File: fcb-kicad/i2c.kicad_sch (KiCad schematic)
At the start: 1 part

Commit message: hierarchic schemas, paljon muuta kivaa
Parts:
- added J3: Conn_01x04_Male, symbol Connector:Conn_01x04_Male
- added R10, R9: 10k, Resistor_SMD:R_0603_1608Metric, symbol Device:R_Small
- gave numbers to parts that had none: 1
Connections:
- new net +3V3: J3.1 (Pin_1), R10.1, R9.1
- new net GND: J3.4 (Pin_4)
- new net I2C1_SCL: J3.2 (Pin_2), J3.3 (Pin_3), R9.2
- new net I2C1_SDA: R10.2
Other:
- note added: "Connector for external I2C devices"
- note added: "Pullups for I2C lines"
- company: (none) -> University of Oulu
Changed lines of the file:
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@@
 (kicad_sch (version 20211123) (generator eeschema)
   (paper "A4")
+  (title_block
+    (company "University of Oulu")
+    (comment 1 "Antti Luukkonen, Jouni Saari, Visa Tuominen")
+  )
+  (wire (pts (xy 45.72 40.64) (xy 45.72 33.02))
+    (stroke (width 0) (type default) (color 0 0 0 0))
+  )
+  (wire (pts (xy 67.945 30.48) (xy 71.12 30.48))
+    (stroke (width 0) (type default) (color 0 0 0 0))
+  )
+  (wire (pts (xy 71.12 38.1) (xy 67.945 38.1))
+    (stroke (width 0) (type default) (color 0 0 0 0))
+  )
+  (wire (pts (xy 38.1 35.56) (xy 38.1 33.02))
+    (stroke (width 0) (type default) (color 0 0 0 0))
+  )
+  (wire (pts (xy 67.945 38.1) (xy 67.945 39.37))
+    (stroke (width 0) (type default) (color 0 0 0 0))
+  )
+  (wire (pts (xy 67.945 29.21) (xy 67.945 30.48))
+    (stroke (width 0) (type default) (color 0 0 0 0))
+  )
+  (wire (pts (xy 34.29 35.56) (xy 38.1 35.56))
+    (stroke (width 0) (type default) (color 0 0 0 0))
+  )
+  (wire (pts (xy 34.29 40.64) (xy 45.72 40.64))
+    (stroke (width 0) (type default) (color 0 0 0 0))
+  )
+  (text "Pullups for I2C lines\n" (at 22.86 21.59 0)
+    (effects (font (size 1.27 1.27)) (justify left bottom))
+  )
+  (text "Connector for external I2C devices" (at 58.42 21.59 0)
+    (effects (font (size 1.27 1.27)) (justify left bottom))
+  )
+  (global_label "I2C1_SCL" (shape input) (at 71.12 33.02 180) (fields_autoplaced)
+    (effects (font (size 1.27 1.27)) (justify right))
+    (property "Intersheet References" "${INTERSHEET_REFS}" (id 0) (at 59.9379 32.9406 0)
+      (effects (font (size 1.27 1.27)) (justify right) hide)
+    )
+  )
+  (global_label "I2C1_SCL" (shape input) (at 34.29 35.56 180) (fields_autoplaced)
+    (effects (font (size 1.27 1.27)) (justify right))
+    (property "Intersheet References" "${INTERSHEET_REFS}" (id 0) (at 23.1079 35.4806 0)
+      (effects (font (size 1.27 1.27)) (justify right) hide)
+    )
+  )
+  (global_label "I2C1_SCL" (shape input) (at 71.12 35.56 180) (fields_autoplaced)
+    (effects (font (size 1.27 1.27)) (justify right))
+    (property "Intersheet References" "${INTERSHEET_REFS}" (id 0) (at 59.9379 35.4806 0)
+      (effects (font (size 1.27 1.27)) (justify right) hide)
+    )
+  )
+  (global_label "I2C1_SDA" (shape input) (at 34.29 40.64 180) (fields_autoplaced)
+    (effects (font (size 1.27 1.27)) (justify right))
+    (property "Intersheet References" "${INTERSHEET_REFS}" (id 0) (at 23.0474 40.5606 0)
+      (effects (font (size 1.27 1.27)) (justify right) hide)
+    )
+  )
+  (symbol (lib_id "Device:R_Small") (at 38.1 30.48 0) (unit 1)
+    (in_bom yes) (on_board yes) (fields_autoplaced)
+    (property "Reference" "R9" (id 0) (at 39.5986 29.5715 0)
+      (effects (font (size 1.27 1.27)) (justify left))
+    )
+    (property "Value" "10k" (id 1) (at 39.5986 32.3466 0)
+      (effects (font (size 1.27 1.27)) (justify left))
+    )
+    (property "Footprint" "Resistor_SMD:R_0603_1608Metric" (id 2) (at 38.1 30.48 0)
+      (effects (font (size 1.27 1.27)) hide)
+    )
+    (property "Datasheet" "~" (id 3) (at 38.1 30.48 0)
+      (effects (font (size 1.27 1.27)) hide)
+    )
+    (property "LCSC" "C25804" (id 4) (at 38.1 30.48 0)
+      (effects (font (size 1.27 1.27)) hide)
+    )
+    (pin "1")
+    (pin "2")
+  )
+  (symbol (lib_id "power:+3.3V") (at 38.1 27.94 0) (unit 1)
+    (in_bom yes) (on_board yes) (fields_autoplaced)
+    (property "Reference" "#PWR021" (id 0) (at 38.1 31.75 0)
+      (effects (font (size 1.27 1.27)) hide)
+    )
+    (property "Value" "+3.3V" (id 1) (at 38.1 24.3355 0))
+    (property "Footprint" "" (id 2) (at 38.1 27.94 0)
+      (effects (font (size 1.27 1.27)) hide)
+    )
+    (property "Datasheet" "" (id 3) (at 38.1 27.94 0)
+      (effects (font (size 1.27 1.27)) hide)
+    )
+    (pin "1")
+  )
   (symbol (lib_id "000_sjt:BMP388") (at 80.01 74.93 0) (unit 1)
     (in_bom yes) (on_board yes) (fields_autoplaced)
-    (property "Reference" "U?" (id 0) (at 80.01 52.07 0))
+    (property "Reference" "U8" (id 0) (at 80.01 52.07 0))
     (property "Value" "BMP388" (id 1) (at 80.01 54.61 0))
     (property "Footprint" "000_sjt:PQFN50P200X200X80-10N" (id 2) (at 80.01 57.15 0))
@@
     (pin "9")
   )
+  (symbol (lib_id "power:GND") (at 67.945 39.37 0) (unit 1)
+    (in_bom yes) (on_board yes) (fields_autoplaced)
+    (property "Reference" "#PWR031" (id 0) (at 67.945 45.72 0)
+      (effects (font (size 1.27 1.27)) hide)
+    )
+    (property "Value" "GND" (id 1) (at 67.945 43.9325 0))
+    (property "Footprint" "" (id 2) (at 67.945 39.37 0)
+      (effects (font (size 1.27 1.27)) hide)
+    )
+    (property "Datasheet" "" (id 3) (at 67.945 39.37 0)
+      (effects (font (size 1.27 1.27)) hide)
+    )
+    (pin "1")
+  )
+  (symbol (lib_id "power:+3.3V") (at 45.72 27.94 0) (unit 1)
+    (in_bom yes) (on_board yes) (fields_autoplaced)
+    (property "Reference" "#PWR024" (id 0) (at 45.72 31.75 0)
+      (effects (font (size 1.27 1.27)) hide)
+    )
+    (property "Value" "+3.3V" (id 1) (at 45.72 24.3355 0))
+    (property "Footprint" "" (id 2) (at 45.72 27.94 0)
+      (effects (font (size 1.27 1.27)) hide)
+    )
+    (property "Datasheet" "" (id 3) (at 45.72 27.94 0)
+      (effects (font (size 1.27 1.27)) hide)
+    )
+    (pin "1")
+  )
+  (symbol (lib_id "Connector:Conn_01x04_Male") (at 76.2 33.02 0) (mirror y) (unit 1)
+    (in_bom yes) (on_board yes) (fields_autoplaced)
+    (property "Reference" "J3" (id 0) (at 76.9112 33.3815 0)
+      (effects (font (size 1.27 1.27)) (justify right))
+    )
+    (property "Value" "Conn_01x04_Male" (id 1) (at 76.9112 36.1566 0)
+      (effects (font (size 1.27 1.27)) (justify right))
+    )
+    (property "Footprint" "" (id 2) (at 76.2 33.02 0)
+      (effects (font (size 1.27 1.27)) hide)
+    )
+    (property "Datasheet" "~" (id 3) (at 76.2 33.02 0)
+      (effects (font (size 1.27 1.27)) hide)
+    )
+    (pin "1")
+    (pin "2")
+    (pin "3")
+    (pin "4")
+  )
+  (symbol (lib_id "Device:R_Small") (at 45.72 30.48 0) (unit 1)
+    (in_bom yes) (on_board yes) (fields_autoplaced)
+    (property "Reference" "R10" (id 0) (at 47.2186 29.5715 0)
+      (effects (font (size 1.27 1.27)) (justify left))
+    )
+    (property "Value" "10k" (id 1) (at 47.2186 32.3466 0)
+      (effects (font (size 1.27 1.27)) (justify left))
+    )
+    (property "Footprint" "Resistor_SMD:R_0603_1608Metric" (id 2) (at 45.72 30.48 0)
+      (effects (font (size 1.27 1.27)) hide)
+    )
+    (property "Datasheet" "~" (id 3) (at 45.72 30.48 0)
+      (effects (font (size 1.27 1.27)) hide)
+    )
+    (property "LCSC" "C25804" (id 4) (at 45.72 30.48 0)
+      (effects (font (size 1.27 1.27)) hide)
+    )
+    (pin "1")
+    (pin "2")
+  )
+  (symbol (lib_id "power:+3.3V") (at 67.945 29.21 0) (unit 1)
+    (in_bom yes) (on_board yes) (fields_autoplaced)
+    (property "Reference" "#PWR025" (id 0) (at 67.945 33.02 0)
+      (effects (font (size 1.27 1.27)) hide)
+    )
+    (property "Value" "+3.3V" (id 1) (at 67.945 25.6055 0))
+    (property "Footprint" "" (id 2) (at 67.945 29.21 0)
+      (effects (font (size 1.27 1.27)) hide)
+    )
+    (property "Datasheet" "" (id 3) (at 67.945 29.21 0)
+      (effects (font (size 1.27 1.27)) hide)
+    )
+    (pin "1")
+  )
 )

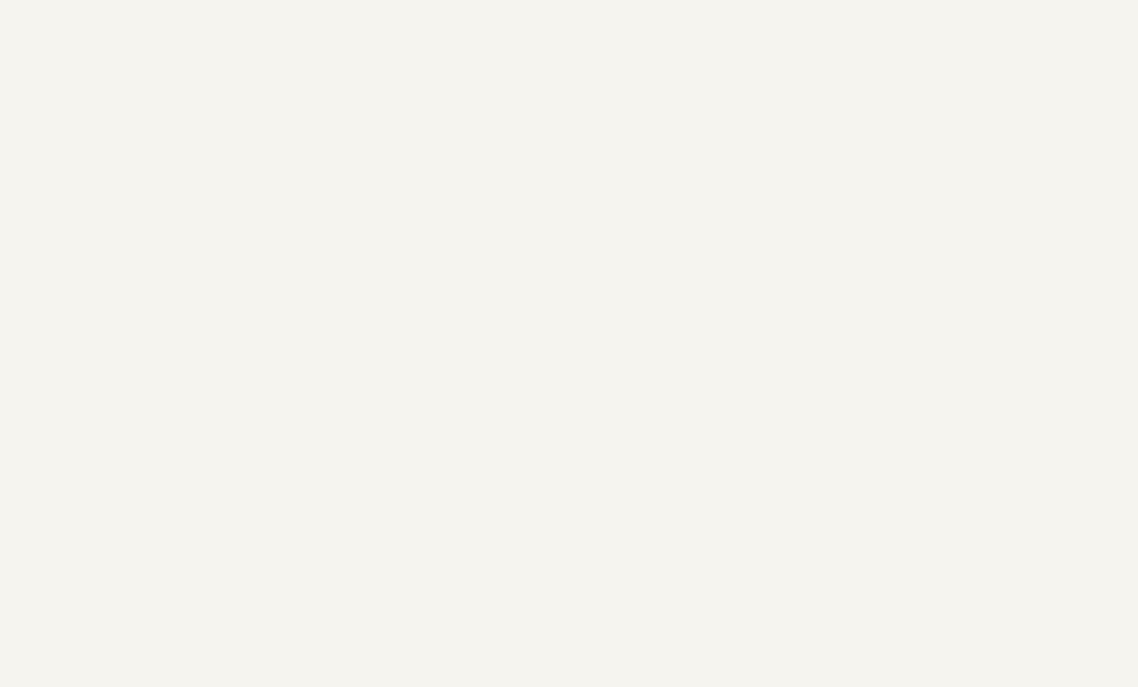
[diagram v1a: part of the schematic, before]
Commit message: 4in1 connector library part, SPI CS pullups, migrate magnetometer cirtuit
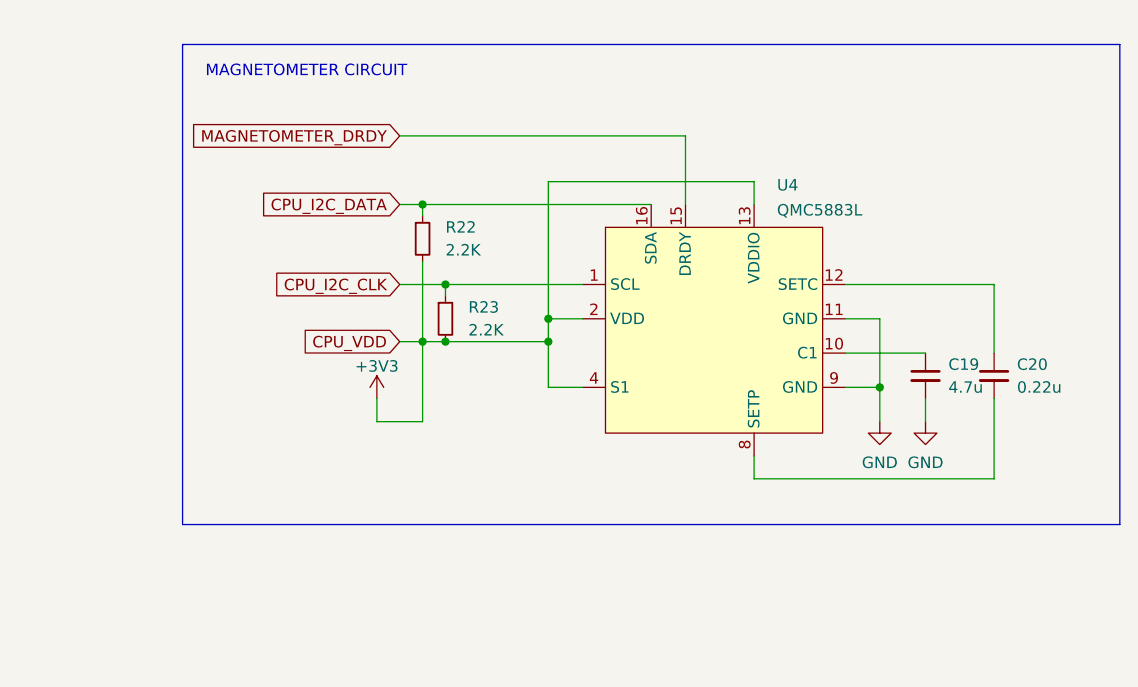
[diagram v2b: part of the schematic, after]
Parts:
- added C19: 4.7u, symbol Device:C_Small
- added C20: 0.22u, symbol Device:C_Small
- added R22, R23: 2.2K, symbol Device:R_Small
- added U4: QMC5883L, symbol 000_sjt:QMC5883L
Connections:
- net +3V3: now also R22.2, R23.2, U4.13 (VDDIO), U4.2 (VDD), U4.4 (S1)
- net GND: now also C19.2, U4.11 (GND), U4.9 (GND)
- new net: C19.1, U4.10 (C1)
- new net: C20.1, U4.12 (SETC)
- new net: C20.2, U4.8 (SETP)
- new net CPU_I2C_CLK: R23.1, U4.1 (SCL)
- new net CPU_I2C_DATA: R22.1, U4.16 (SDA)
- new net MAGNETOMETER_DRDY: U4.15 (DRDY)
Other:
- note added: "MAGNETOMETER CIRCUIT"

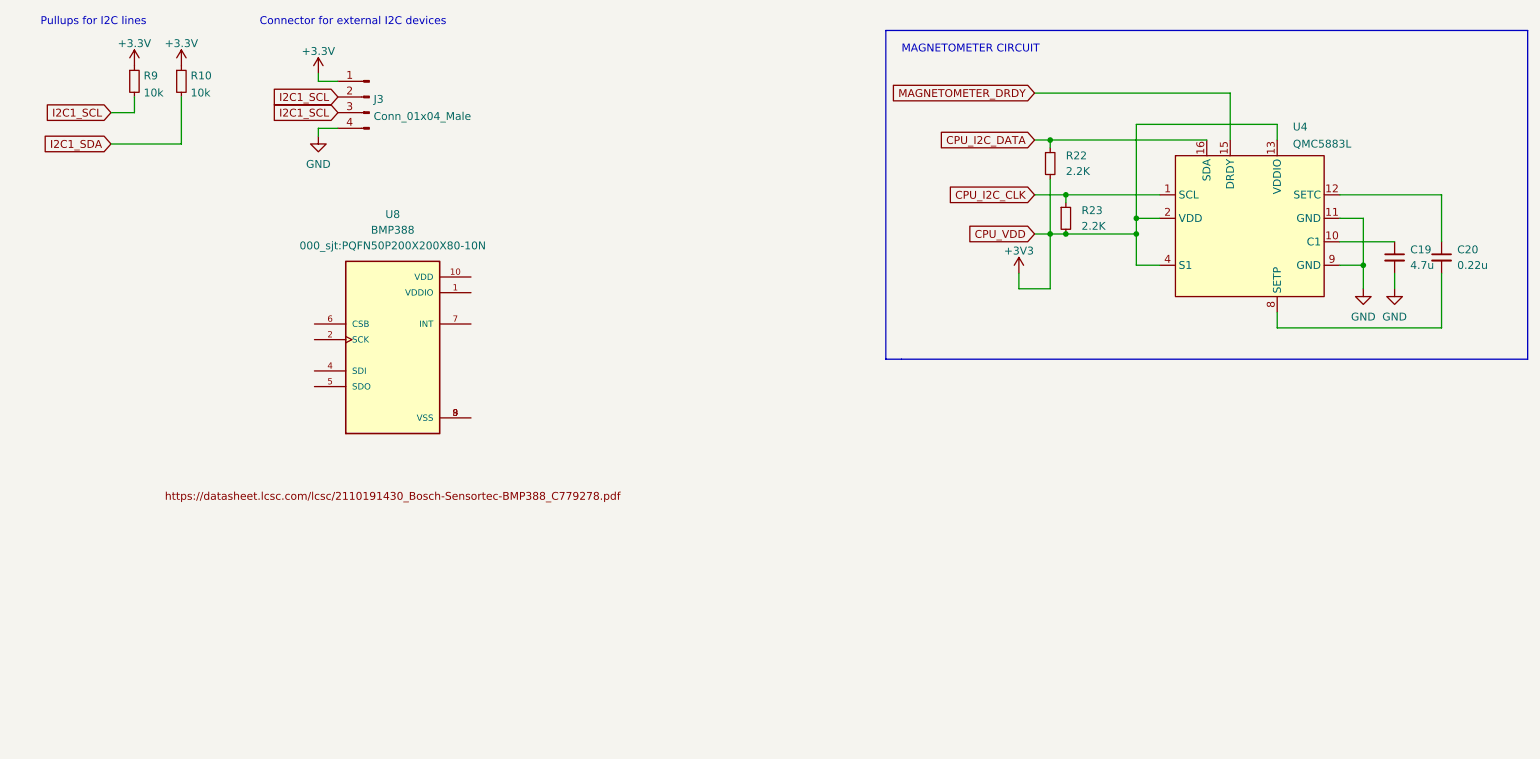
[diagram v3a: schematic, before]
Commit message: Schema rev0 done, Layout components grouped
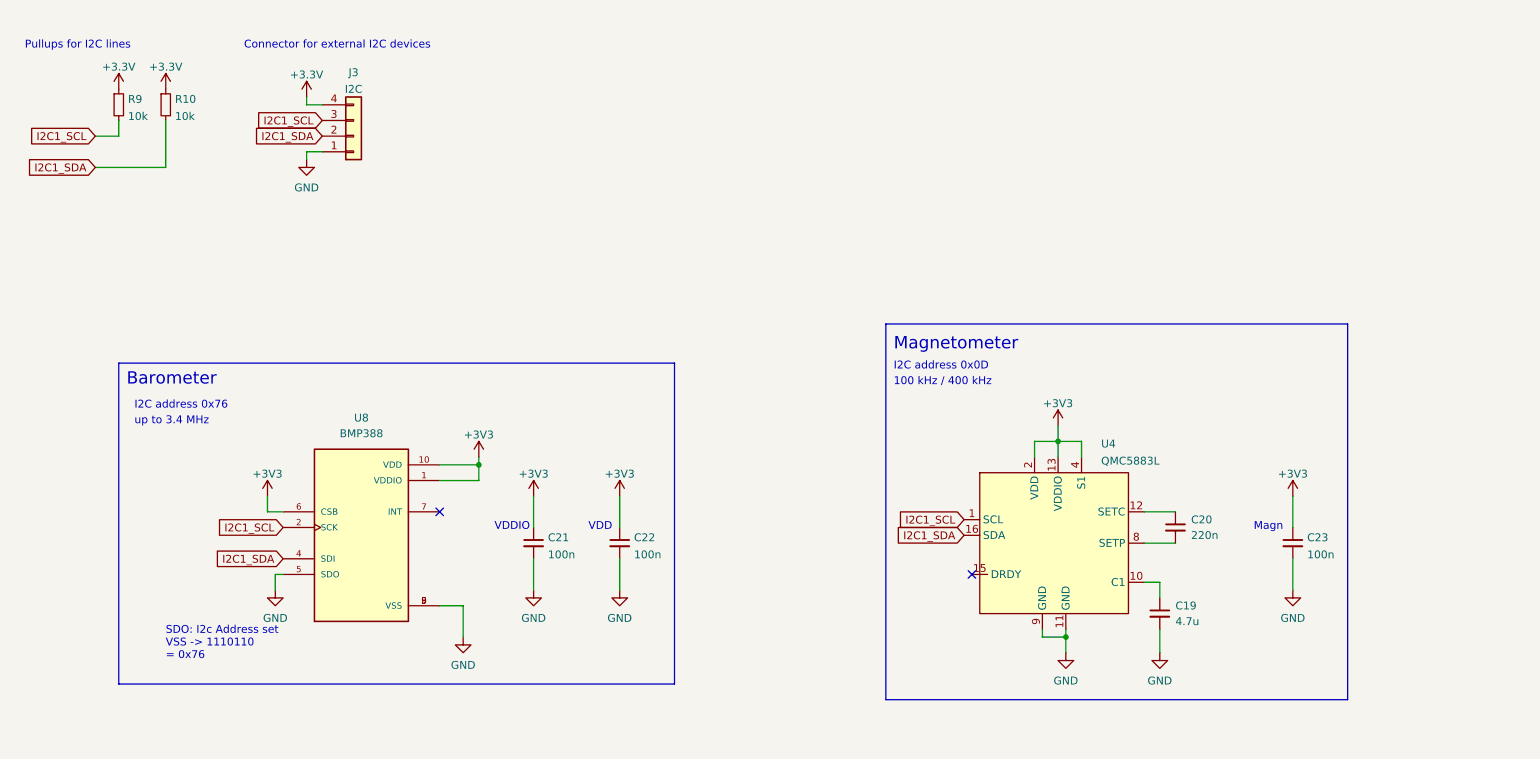
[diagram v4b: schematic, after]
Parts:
- removed R22, R23: 2.2K, symbol Device:R_Small
- added C21, C22, C23: 100n, Capacitor_SMD:C_0603_1608Metric, symbol Device:C_Small
- C19: footprint (none) -> Capacitor_SMD:C_0603_1608Metric
- C20: value 0.22u -> 220n; footprint (none) -> Capacitor_SMD:C_0603_1608Metric
- J3: value Conn_01x04_Male -> I2C; footprint (none) -> Connector_PinHeader_2.00mm:PinHeader_1x04_P2.00mm_Vertical; symbol Connector:Conn_01x04_Male -> Connector_Generic:Conn_01x04
- U4: footprint (none) -> 000_sjt:QMC5883L
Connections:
- net CPU_I2C_CLK is gone; now on net I2C1_SCL: U4.1 (SCL)
- net CPU_I2C_DATA is gone; now on net I2C1_SDA: U4.16 (SDA)
- net +3V3: now also J3.4 (Pin_4), U8.1 (VDDIO), U8.10 (VDD), U8.6 (CSB), C21.1, C22.1, C23.1; no longer J3.1 (Pin_1)
- net GND: now also J3.1 (Pin_1), U8.3 (VSS), U8.5 (SDO), U8.8 (VSS), U8.9 (VSS), C21.2, C22.2, C23.2; no longer J3.4 (Pin_4)
- net I2C1_SCL: now also U8.2 (SCK); no longer J3.2 (Pin_2)
- net I2C1_SDA: now also J3.2 (Pin_2), U8.4 (SDI)
- net MAGNETOMETER_DRDY: no longer names the net of U4.15 (DRDY)
- no-connect marks 0 -> 2
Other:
- note added: "100 kHz / 400 kHz"
- note added: "Barometer"
- note added: "I2C address 0x0D"
- note added: "I2C address 0x76"
- note added: "Magn"
- note added: "Magnetometer"
- note added: "SDO: I2c Address set VSS -> 1110110 = 0x76"
- note added: "VDD"
- note added: "VDDIO"
- note added: "up to 3.4 MHz"
- note removed: "MAGNETOMETER CIRCUIT"
- title: (none) -> I2C peripherials
- moved on the sheet: C19, C20, R10, R9, U4
